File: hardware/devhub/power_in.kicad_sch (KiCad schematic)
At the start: 24 parts, among them J1 USB-C PWR IN, U1 AP7361C-33E, U13 TPS259470ARPWR

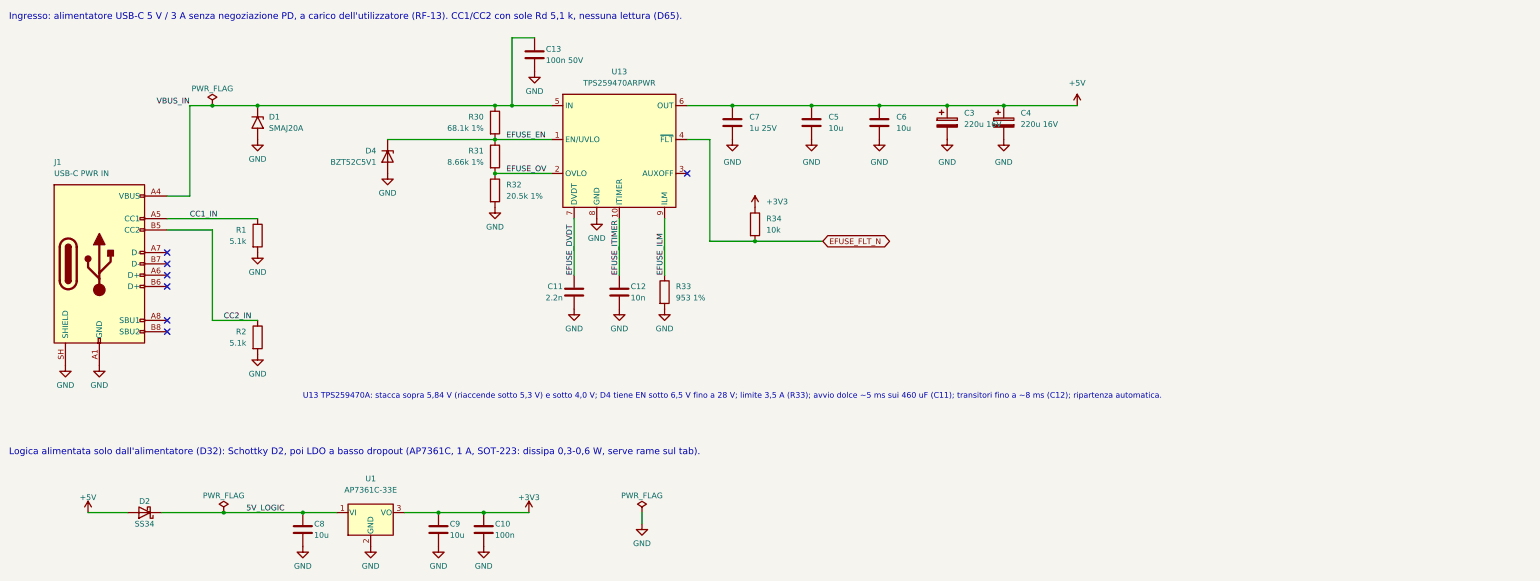
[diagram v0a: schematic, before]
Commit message: PCB routing complete, package in values, MPN fields
- Routing finished; ESD_FANOUT rule area for D20 centre pins
- Vias keep inner-layer rings only where connected; GND reference vias
  next to SWD and I2C layer changes
- Value field of chip R/C/LED includes the package (0402...1206)
- New fields MPN lcsc, MPN mouser, MPN digikey; LCSC codes for R60/R61,
  U3, U4/U5 and supplier codes completed; JP2 marked DNP on the PCB
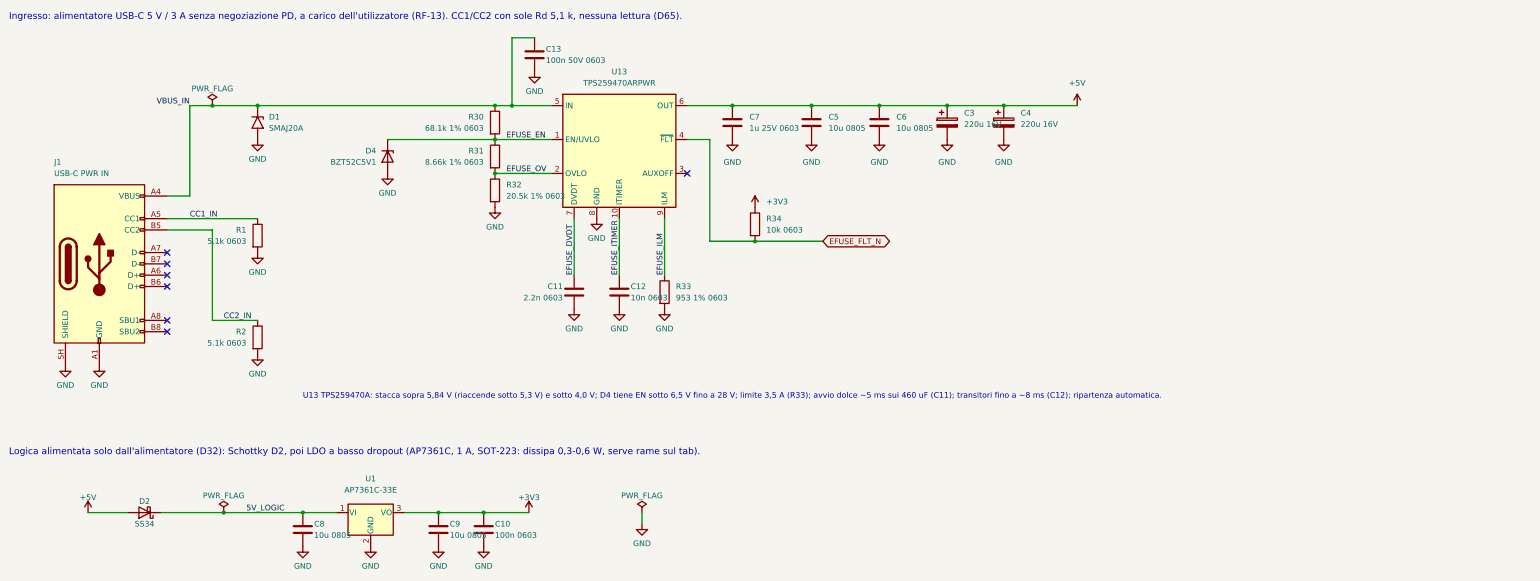
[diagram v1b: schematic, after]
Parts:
- C10: value 100n -> 100n 0603; MPN digikey (none) -> CL10B104KB8NNNC; MPN lcsc (none) -> CL10B104KB8NNNC; MPN mouser (none) -> CL10B104KB8NNNC
- C11: value 2.2n -> 2.2n 0603; MPN digikey (none) -> CL10B222KB8NNNC; MPN lcsc (none) -> CL10B222KB8NNNC; MPN mouser (none) -> CL10B222KB8NNNC
- C12: value 10n -> 10n 0603; MPN digikey (none) -> CL10B103KB8NNNC; MPN lcsc (none) -> CL10B103KB8NNNC; MPN mouser (none) -> CL10B103KB8NNNC
- C13: value 100n 50V -> 100n 50V 0603; MPN digikey (none) -> CL10B104KB8NNNC; MPN lcsc (none) -> CL10B104KB8NNNC; MPN mouser (none) -> CL10B104KB8NNNC
- C3, C4: MPN digikey (none) -> EEE-FK1C221XP; MPN lcsc (none) -> EEE-FK1C221XP; MPN mouser (none) -> EEE-FK1C221XP
- C5, C6, C8, C9: value 10u -> 10u 0805; MPN digikey (none) -> GRM21BR61H106KE43L; MPN lcsc (none) -> GRM21BR61H106KE43L; MPN mouser (none) -> GRM21BR61H106KE43L
- C7: value 1u 25V -> 1u 25V 0603; MPN digikey (none) -> CL10B105KA8NNNC; MPN lcsc (none) -> CL10B105KA8NNNC; MPN mouser (none) -> CL10B105KA8NNNC
- D1: MPN digikey (none) -> SMAJ20A-13-F; MPN lcsc (none) -> SMAJ20A-13-F; MPN mouser (none) -> SMAJ20A-13-F
- D2: MPN digikey (none) -> B340A-13-F; MPN lcsc (none) -> B340A-13-F; MPN mouser (none) -> B340A-13-F
- D4: MPN digikey (none) -> BZT52C5V1-7-F; MPN lcsc (none) -> BZT52C5V1-7-F; MPN mouser (none) -> BZT52C5V1-7-F
- J1: MPN digikey (none) -> USB4105-GF-A; MPN lcsc (none) -> USB4105-GF-A; MPN mouser (none) -> USB4105-GF-A
- R1, R2: value 5.1k -> 5.1k 0603; MPN digikey (none) -> RC0603FR-075K1L; MPN lcsc (none) -> 0603WAF5101T5E; MPN mouser (none) -> RC0603FR-075K1L
- R30: value 68.1k 1% -> 68.1k 1% 0603; MPN digikey (none) -> RC0603FR-0768K1L; MPN lcsc (none) -> RC0603FR-0768K1L; MPN mouser (none) -> RC0603FR-0768K1L
- R31: value 8.66k 1% -> 8.66k 1% 0603; MPN digikey (none) -> RC0603FR-078K66L; MPN lcsc (none) -> 0603WAF8661T5E; MPN mouser (none) -> RC0603FR-078K66L
- R32: value 20.5k 1% -> 20.5k 1% 0603; MPN digikey (none) -> RC0603FR-0720K5L; MPN lcsc (none) -> RC0603FR-0720K5L; MPN mouser (none) -> RC0603FR-0720K5L
- R33: value 953 1% -> 953 1% 0603; MPN digikey (none) -> RC0603FR-07953RL; MPN lcsc (none) -> RC0603FR-07953RL; MPN mouser (none) -> RC0603FR-07953RL
- R34: value 10k -> 10k 0603; MPN digikey (none) -> RC0603FR-0710KL; MPN lcsc (none) -> FRC0603F1002TS; MPN mouser (none) -> RC0603FR-0710KL
- U1: MPN digikey (none) -> AP7361C-33E-13; MPN lcsc (none) -> AP7361C-33E-13; MPN mouser (none) -> AP7361C-33E-13
- U13: MPN digikey (none) -> TPS259470ARPWR; MPN lcsc (none) -> TPS259470ARPWR; MPN mouser (none) -> TPS259470ARPWR

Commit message: D4: use Vishay BZT52C5V1-G3-18 for Mouser and DigiKey
BZT52C5V1-7-F stays the LCSC part; same 5.1 V SOD-123 footprint.
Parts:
- D4: MPN digikey BZT52C5V1-7-F -> BZT52C5V1-G3-18; MPN mouser BZT52C5V1-7-F -> BZT52C5V1-G3-18; digikey BZT52C5V1-FDICT-ND -> 112-BZT52C5V1-G3-18CT-ND; mouser 621-BZT52C5V1-F -> 78-BZT52C5V1-G3-18
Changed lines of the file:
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@@
 			)
 		)
-		(property "mouser" "621-BZT52C5V1-F"
+		(property "mouser" "78-BZT52C5V1-G3-18"
 			(at 95.25 46.99 270)
 			(hide yes)
@@
 			)
 		)
-		(property "digikey" "BZT52C5V1-FDICT-ND"
+		(property "digikey" "112-BZT52C5V1-G3-18CT-ND"
 			(at 95.25 46.99 270)
 			(hide yes)
@@
 			)
 		)
-		(property "MPN mouser" "BZT52C5V1-7-F"
+		(property "MPN mouser" "BZT52C5V1-G3-18"
 			(at 95.25 46.99 270)
 			(hide yes)
@@
 			)
 		)
-		(property "MPN digikey" "BZT52C5V1-7-F"
+		(property "MPN digikey" "BZT52C5V1-G3-18"
 			(at 95.25 46.99 270)
 			(hide yes)

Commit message: U1: switch to AP7361C-33ER (SOT-223R) for Mouser availability (D91)
- Project symbol devhub:AP7361C-33ER: pin 1 GND, pin 2 and tab OUT, pin 3 IN
- U1 supplier codes: LCSC C3743528, Mouser 621-AP7361C-33ER-13, DigiKey AP7361C-33ER-13DICT-ND
- PCB updated for the reversed pinout; U1_HEATSINK on +3V3
- Docs aligned: components, costs, architecture, PCB rules, decision D91
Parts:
- U1: value AP7361C-33E -> AP7361C-33ER; symbol Regulator_Linear:AP7361C-33E -> devhub:AP7361C-33ER; MPN digikey AP7361C-33E-13 -> AP7361C-33ER-13; MPN lcsc AP7361C-33E-13 -> AP7361C-33ER-13; MPN mouser AP7361C-33E-13 -> AP7361C-33ER-13; digikey AP7361C-33E-13DICT-ND -> AP7361C-33ER-13DICT-ND; lcsc C500795 -> C3743528; mouser 621-AP7361C-33E-13 -> 621-AP7361C-33ER-13
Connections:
- net +3V3: now also U1.2 (VO); no longer U1.3 (VO)
- net 5V_LOGIC: now also U1.3 (VI); no longer U1.1 (VI)
- net GND: now also U1.1 (GND); no longer U1.2 (GND)
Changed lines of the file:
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@@
 	)
 	(symbol
-		(lib_id "Regulator_Linear:AP7361C-33E")
+		(lib_id "devhub:AP7361C-33ER")
 		(at 91.44 127 0)
 		(unit 1)
@@
 			)
 		)
-		(property "Value" "AP7361C-33E"
+		(property "Value" "AP7361C-33ER"
 			(at 91.44 121.92 0)
 			(show_name no)
@@
 			)
 		)
-		(property "Description" "1A Low Dropout regulator, positive, 3.3V fixed output, SOT-223"
+		(property "Description" "1A Low Dropout regulator, positive, 3.3V fixed output, SOT-223R (pin 1 GND, tab/pin 2 VO, pin 3 VI)"
 			(at 91.44 127 0)
 			(hide yes)
@@
 			)
 		)
-		(property "lcsc" "C500795"
+		(property "lcsc" "C3743528"
 			(at 91.44 127 0)
 			(hide yes)
@@
 			)
 		)
-		(property "mouser" "621-AP7361C-33E-13"
+		(property "mouser" "621-AP7361C-33ER-13"
 			(at 91.44 127 0)
 			(hide yes)
@@
 			)
 		)
-		(property "digikey" "AP7361C-33E-13DICT-ND"
+		(property "digikey" "AP7361C-33ER-13DICT-ND"
 			(at 91.44 127 0)
 			(hide yes)
@@
 			)
 		)
-		(property "MPN lcsc" "AP7361C-33E-13"
+		(property "MPN lcsc" "AP7361C-33ER-13"
 			(at 91.44 127 0)
 			(hide yes)
@@
 			)
 		)
-		(property "MPN mouser" "AP7361C-33E-13"
+		(property "MPN mouser" "AP7361C-33ER-13"
 			(at 91.44 127 0)
 			(hide yes)
@@
 			)
 		)
-		(property "MPN digikey" "AP7361C-33E-13"
+		(property "MPN digikey" "AP7361C-33ER-13"
 			(at 91.44 127 0)
 			(hide yes)

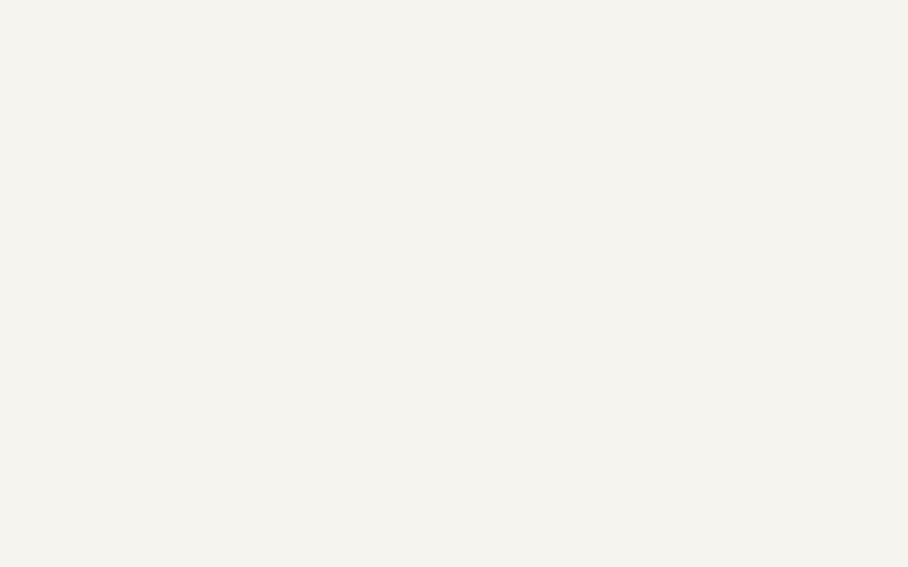
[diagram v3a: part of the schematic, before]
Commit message: Test points, LED host moved, board finished (D92)
- 14 test points: GND loops TP1/TP10 (Keystone 5001), pads for +5V, +3V3,
  I2C1/I2C2, HUB_RST_N, EFUSE_FLT_N and VBUS_P1-P4
- D93/R93 moved to the rear, left of J1
- Button symbols: generic Value, function in Description; PCB aligned
- Docs: decision D92, components, PCB test rules, LED host position
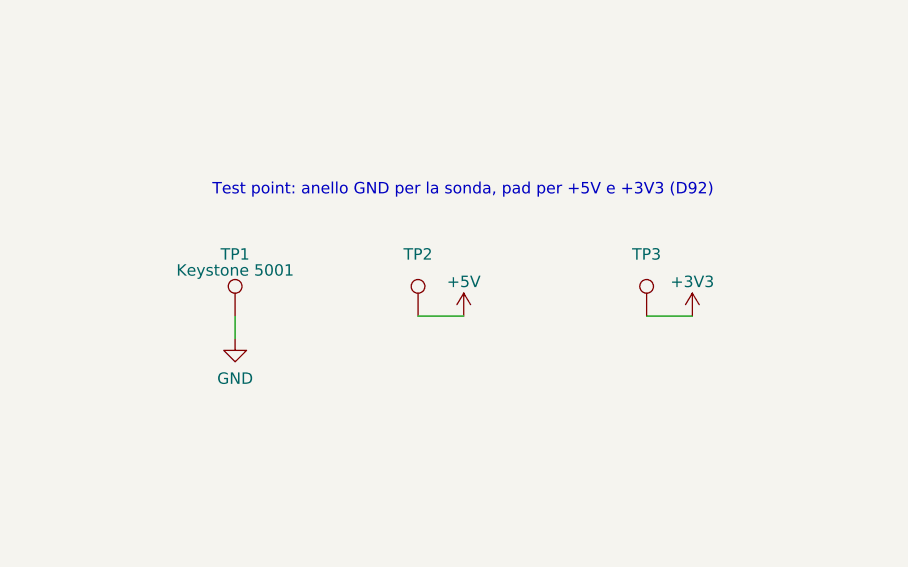
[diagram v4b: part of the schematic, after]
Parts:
- added TP1: Keystone 5001, TestPoint:TestPoint_Keystone_5000-5004_Miniature, symbol Connector:TestPoint
- added TP2: +5V, TestPoint:TestPoint_Pad_D1.5mm, symbol Connector:TestPoint
- added TP3: +3V3, TestPoint:TestPoint_Pad_D1.5mm, symbol Connector:TestPoint
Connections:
- net +3V3: now also TP3.1
- net +5V: now also TP2.1
- net GND: now also TP1.1
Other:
- note added: "Test point: anello GND per la sonda, pad per +5V e +3V3 (D92)"
